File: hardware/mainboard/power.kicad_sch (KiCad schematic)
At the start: 18 parts, among them J105 Eurorack Power, U1 LM4040DBZ-10, U2 LD1117-3.3

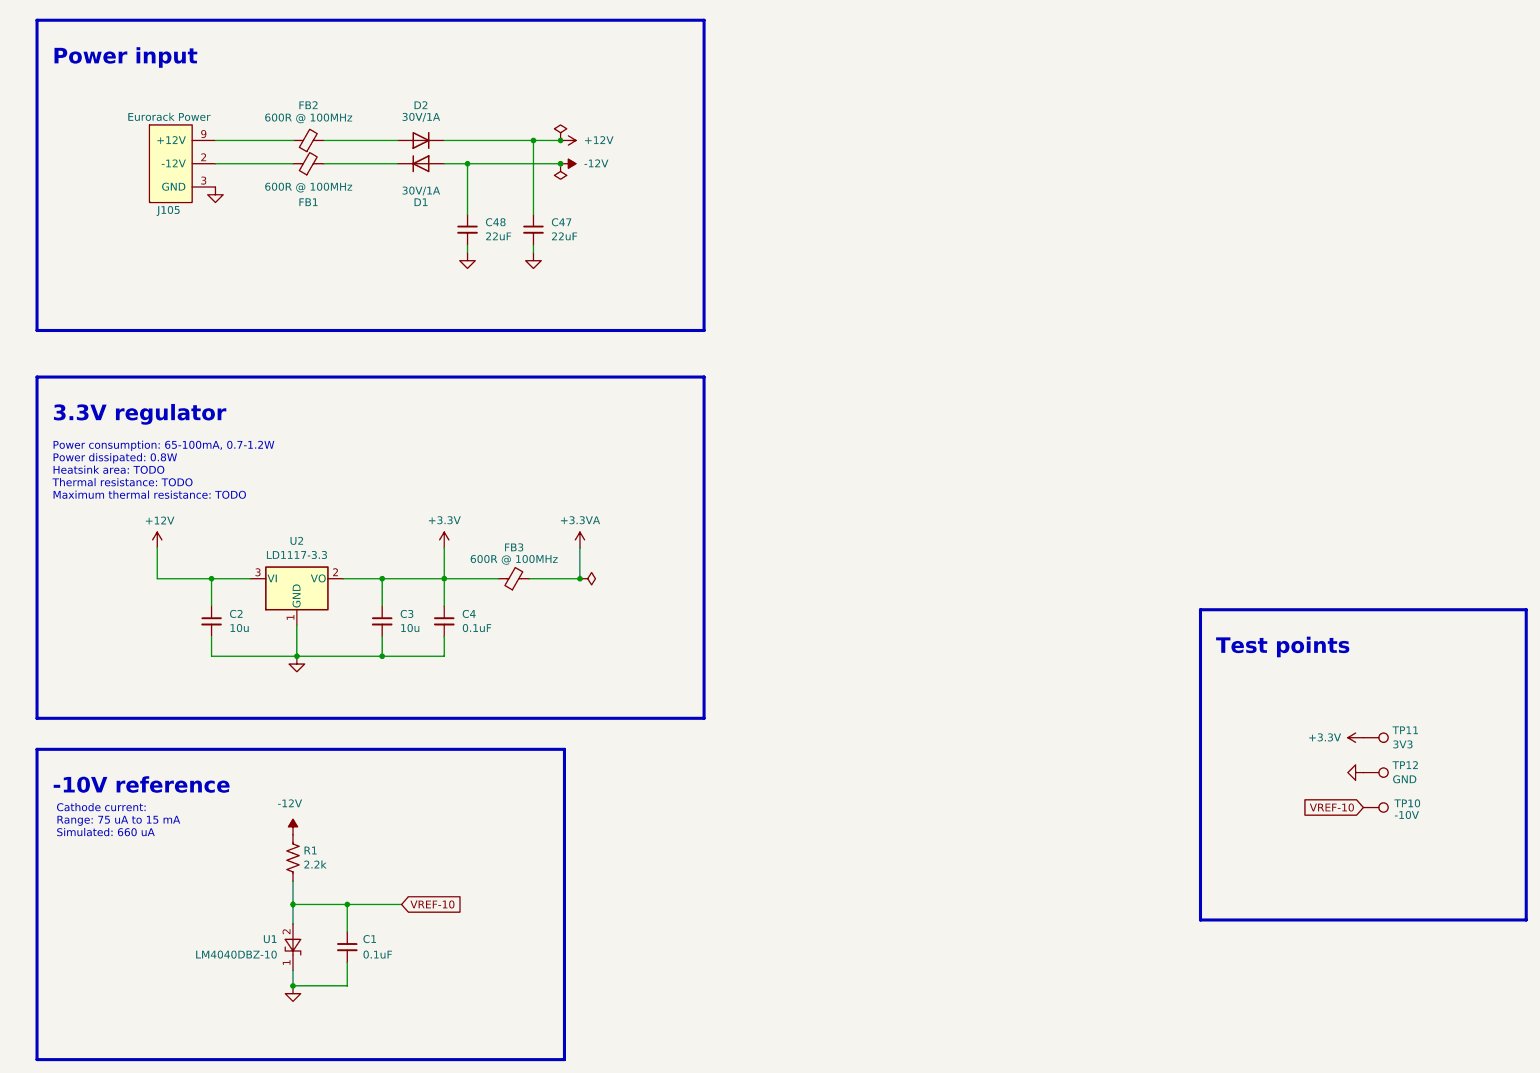
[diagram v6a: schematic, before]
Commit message: Reannotate schematic
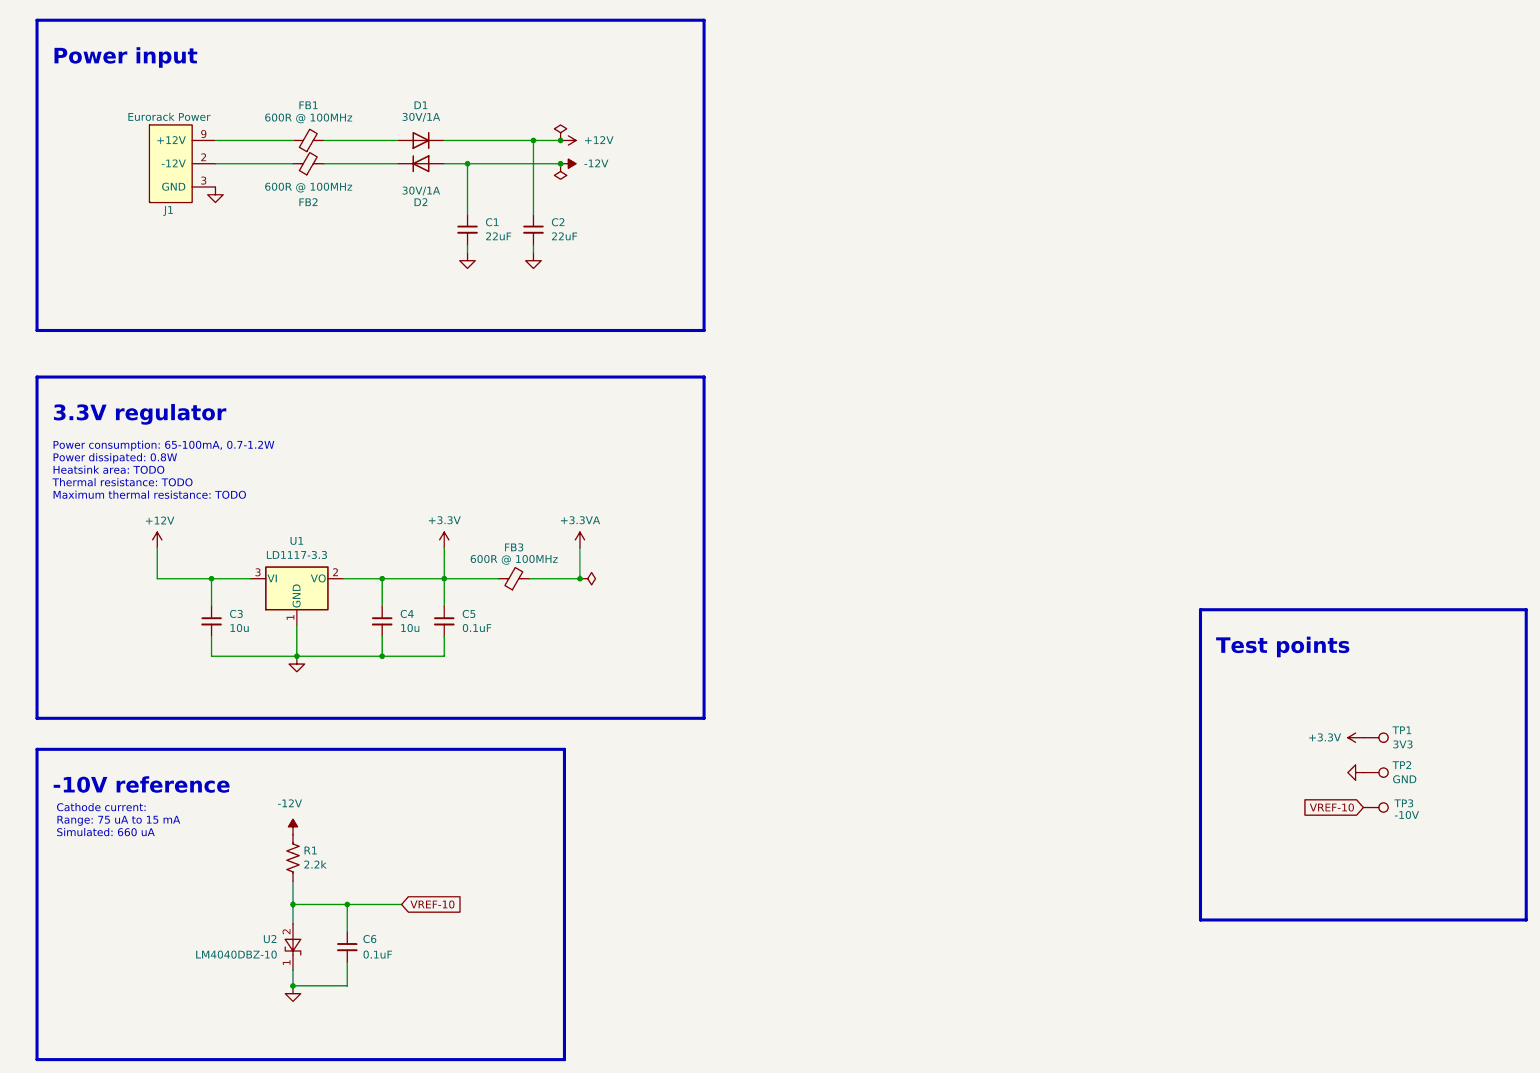
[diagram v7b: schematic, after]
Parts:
- renumbered C48 to C1, C47 to C2, C2 to C3, C3 to C4, C4 to C5, C1 to C6, D2 to D1, D1 to D2, FB2 to FB1, FB1 to FB2, J105 to J1, TP11 to TP1, TP12 to TP2, TP10 to TP3, U2 to U1, U1 to U2
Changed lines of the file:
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@@
   (symbol (lib_id "Device:D") (at 80.645 41.275 0) (unit 1)
     (in_bom yes) (on_board yes)
-    (property "Reference" "D1" (id 0) (at 80.645 47.625 0))
+    (property "Reference" "D2" (id 0) (at 80.645 47.625 0))
     (property "Value" "30V/1A" (id 1) (at 80.645 45.72 0))
     (property "Footprint" "winterbloom:D_SOD-123" (id 2) (at 80.645 41.275 0)
@@
   (symbol (lib_id "Device:D") (at 80.645 37.465 180) (unit 1)
     (in_bom yes) (on_board yes)
-    (property "Reference" "D2" (id 0) (at 80.645 31.75 0))
+    (property "Reference" "D1" (id 0) (at 80.645 31.75 0))
     (property "Value" "30V/1A" (id 1) (at 80.645 33.655 0))
     (property "Footprint" "winterbloom:D_SOD-123" (id 2) (at 80.645 37.465 0)
@@
   (symbol (lib_id "power:+12V") (at 103.505 37.465 270) (unit 1)
     (in_bom yes) (on_board yes)
-    (property "Reference" "#PWR06" (id 0) (at 99.695 37.465 0)
+    (property "Reference" "#PWR04" (id 0) (at 99.695 37.465 0)
       (effects (font (size 1.27 1.27)) hide)
     )
@@
   (symbol (lib_id "Regulator_Linear:LM1117-3.3") (at 60.325 109.22 0) (unit 1)
     (in_bom yes) (on_board yes)
-    (property "Reference" "U2" (id 0) (at 60.325 103.0732 0))
+    (property "Reference" "U1" (id 0) (at 60.325 103.0732 0))
     (property "Value" "LD1117-3.3" (id 1) (at 60.325 105.3846 0))
     (property "Footprint" "Package_TO_SOT_SMD:TO-252-3_TabPin2" (id 2) (at 60.325 109.22 0)
@@
   (symbol (lib_id "Device:C_Small") (at 46.355 116.205 0) (unit 1)
     (in_bom yes) (on_board yes)
-    (property "Reference" "C2" (id 0) (at 49.276 115.0366 0)
+    (property "Reference" "C3" (id 0) (at 49.276 115.0366 0)
       (effects (font (size 1.27 1.27)) (justify left))
     )
@@
   (symbol (lib_id "Device:C_Small") (at 74.295 116.205 0) (unit 1)
     (in_bom yes) (on_board yes)
-    (property "Reference" "C3" (id 0) (at 77.216 115.0366 0)
+    (property "Reference" "C4" (id 0) (at 77.216 115.0366 0)
       (effects (font (size 1.27 1.27)) (justify left))
     )
@@
   (symbol (lib_id "Device:C_Small") (at 84.455 116.205 0) (unit 1)
     (in_bom yes) (on_board yes)
-    (property "Reference" "C4" (id 0) (at 87.376 115.0366 0)
+    (property "Reference" "C5" (id 0) (at 87.376 115.0366 0)
       (effects (font (size 1.27 1.27)) (justify left))
     )
@@
   (symbol (lib_id "power:+3.3V") (at 84.455 104.14 0) (unit 1)
     (in_bom yes) (on_board yes)
-    (property "Reference" "#PWR012" (id 0) (at 84.455 107.95 0)
+    (property "Reference" "#PWR08" (id 0) (at 84.455 107.95 0)
       (effects (font (size 1.27 1.27)) hide)
     )
@@
   (symbol (lib_id "power:+3.3VA") (at 106.68 104.14 0) (unit 1)
     (in_bom yes) (on_board yes)
-    (property "Reference" "#PWR014" (id 0) (at 106.68 107.95 0)
+    (property "Reference" "#PWR09" (id 0) (at 106.68 107.95 0)
       (effects (font (size 1.27 1.27)) hide)
     )
@@
   (symbol (lib_id "power:GND") (at 60.325 121.92 0) (unit 1)
     (in_bom yes) (on_board yes)
-    (property "Reference" "#PWR09" (id 0) (at 60.325 128.27 0)
+    (property "Reference" "#PWR07" (id 0) (at 60.325 128.27 0)
       (effects (font (size 1.27 1.27)) hide)
     )
@@
   (symbol (lib_id "power:+12V") (at 37.465 104.14 0) (unit 1)
     (in_bom yes) (on_board yes)
-    (property "Reference" "#PWR08" (id 0) (at 37.465 107.95 0)
+    (property "Reference" "#PWR06" (id 0) (at 37.465 107.95 0)
       (effects (font (size 1.27 1.27)) hide)
     )
@@
   (symbol (lib_id "Device:FerriteBead_Small") (at 62.23 41.275 90) (unit 1)
     (in_bom yes) (on_board yes)
-    (property "Reference" "FB1" (id 0) (at 62.23 47.625 90))
+    (property "Reference" "FB2" (id 0) (at 62.23 47.625 90))
     (property "Value" "600R @ 100MHz" (id 1) (at 62.23 45.085 90))
     (property "Footprint" "Inductor_SMD:L_0603_1608Metric_Pad1.05x0.95mm_HandSolder" (id 2) (at 62.23 43.053 90)
@@
   (symbol (lib_id "Device:FerriteBead_Small") (at 62.23 37.465 90) (unit 1)
     (in_bom yes) (on_board yes)
-    (property "Reference" "FB2" (id 0) (at 62.23 31.75 90))
+    (property "Reference" "FB1" (id 0) (at 62.23 31.75 90))
     (property "Value" "600R @ 100MHz" (id 1) (at 62.23 33.7566 90))
     (property "Footprint" "Inductor_SMD:L_0603_1608Metric_Pad1.05x0.95mm_HandSolder" (id 2) (at 62.23 39.243 90)
@@
   (symbol (lib_id "winterbloom:LM4040DBZ-10") (at 59.69 169.545 270) (unit 1)
     (in_bom yes) (on_board yes)
-    (property "Reference" "U1" (id 0) (at 57.15 168.275 90)
+    (property "Reference" "U2" (id 0) (at 57.15 168.275 90)
       (effects (font (size 1.27 1.27)) (justify right))
     )
@@
   (symbol (lib_id "power:-12V") (at 59.69 151.13 0) (unit 1)
     (in_bom yes) (on_board yes)
-    (property "Reference" "#PWR03" (id 0) (at 59.69 148.59 0)
+    (property "Reference" "#PWR010" (id 0) (at 59.69 148.59 0)
       (effects (font (size 1.27 1.27)) hide)
     )
@@
   (symbol (lib_id "power:GND") (at 59.69 175.895 0) (unit 1)
     (in_bom yes) (on_board yes)
-    (property "Reference" "#PWR04" (id 0) (at 59.69 182.245 0)
+    (property "Reference" "#PWR011" (id 0) (at 59.69 182.245 0)
       (effects (font (size 1.27 1.27)) hide)
     )
@@
   (symbol (lib_id "Device:C_Small") (at 68.58 169.545 0) (unit 1)
     (in_bom yes) (on_board yes)
-    (property "Reference" "C1" (id 0) (at 71.12 168.275 0)
+    (property "Reference" "C6" (id 0) (at 71.12 168.275 0)
       (effects (font (size 1.27 1.27)) (justify left))
     )
@@
   (symbol (lib_id "Device:C_Small") (at 88.265 52.07 0) (unit 1)
     (in_bom yes) (on_board yes)
-    (property "Reference" "C48" (id 0) (at 91.186 50.9016 0)
+    (property "Reference" "C1" (id 0) (at 91.186 50.9016 0)
       (effects (font (size 1.27 1.27)) (justify left))
     )
@@
   (symbol (lib_id "power:GND") (at 46.99 45.085 0) (unit 1)
     (in_bom yes) (on_board yes)
-    (property "Reference" "#PWR0143" (id 0) (at 46.99 51.435 0)
+    (property "Reference" "#PWR01" (id 0) (at 46.99 51.435 0)
       (effects (font (size 1.27 1.27)) hide)
     )
@@
   (symbol (lib_id "power:PWR_FLAG") (at 106.68 109.22 270) (unit 1)
     (in_bom yes) (on_board yes)
-    (property "Reference" "#FLG0104" (id 0) (at 108.585 109.22 0)
+    (property "Reference" "#FLG03" (id 0) (at 108.585 109.22 0)
       (effects (font (size 1.27 1.27)) hide)
     )
@@
   (symbol (lib_id "power:GND") (at 234.95 140.97 270) (unit 1)
     (in_bom yes) (on_board yes)
-    (property "Reference" "#PWR039" (id 0) (at 228.6 140.97 0)
+    (property "Reference" "#PWR013" (id 0) (at 228.6 140.97 0)
       (effects (font (size 1.27 1.27)) hide)
     )
@@
   (symbol (lib_id "power:+3.3V") (at 234.95 135.255 90) (unit 1)
     (in_bom yes) (on_board yes)
-    (property "Reference" "#PWR038" (id 0) (at 238.76 135.255 0)
+    (property "Reference" "#PWR012" (id 0) (at 238.76 135.255 0)
       (effects (font (size 1.27 1.27)) hide)
     )
@@
   (symbol (lib_id "Connector:TestPoint") (at 234.95 146.685 270) (unit 1)
     (in_bom yes) (on_board yes)
-    (property "Reference" "TP10" (id 0) (at 240.03 146.05 90)
+    (property "Reference" "TP3" (id 0) (at 240.03 146.05 90)
       (effects (font (size 1.27 1.27)) (justify left))
     )
@@
   (symbol (lib_id "Connector:TestPoint") (at 234.95 135.255 270) (unit 1)
     (in_bom yes) (on_board yes)
-    (property "Reference" "TP11" (id 0) (at 239.7252 134.0866 90)
+    (property "Reference" "TP1" (id 0) (at 239.7252 134.0866 90)
       (effects (font (size 1.27 1.27)) (justify left))
     )
@@
   (symbol (lib_id "winterbloom:Eurorack_Power") (at 39.37 41.275 0) (unit 1)
     (in_bom yes) (on_board yes)
-    (property "Reference" "J105" (id 0) (at 39.37 48.895 0))
+    (property "Reference" "J1" (id 0) (at 39.37 48.895 0))
     (property "Value" "Eurorack Power" (id 1) (at 39.37 33.655 0))
     (property "Footprint" "winterbloom:Eurorack_Power_2x5_Shrouded" (id 2) (at 39.37 29.845 0)
@@
   (symbol (lib_id "power:GND") (at 99.06 55.88 0) (unit 1)
     (in_bom yes) (on_board yes)
-    (property "Reference" "#PWR01" (id 0) (at 99.06 62.23 0)
+    (property "Reference" "#PWR03" (id 0) (at 99.06 62.23 0)
       (effects (font (size 1.27 1.27)) hide)
     )
@@
   (symbol (lib_id "Device:C_Small") (at 99.06 52.07 0) (unit 1)
     (in_bom yes) (on_board yes)
-    (property "Reference" "C47" (id 0) (at 101.981 50.9016 0)
+    (property "Reference" "C2" (id 0) (at 101.981 50.9016 0)
       (effects (font (size 1.27 1.27)) (justify left))
     )
@@
   (symbol (lib_id "Connector:TestPoint") (at 234.95 140.97 270) (unit 1)
     (in_bom yes) (on_board yes)
-    (property "Reference" "TP12" (id 0) (at 239.7252 139.8016 90)
-      (effects (font (size 1.27 1.27)) (justify left))
-    )
+    (property "Reference" "TP2" (id 0) (at 239.7252 139.8016 90)
+      (effects (font (size 1.27 1.27)) (justify left))
+    )

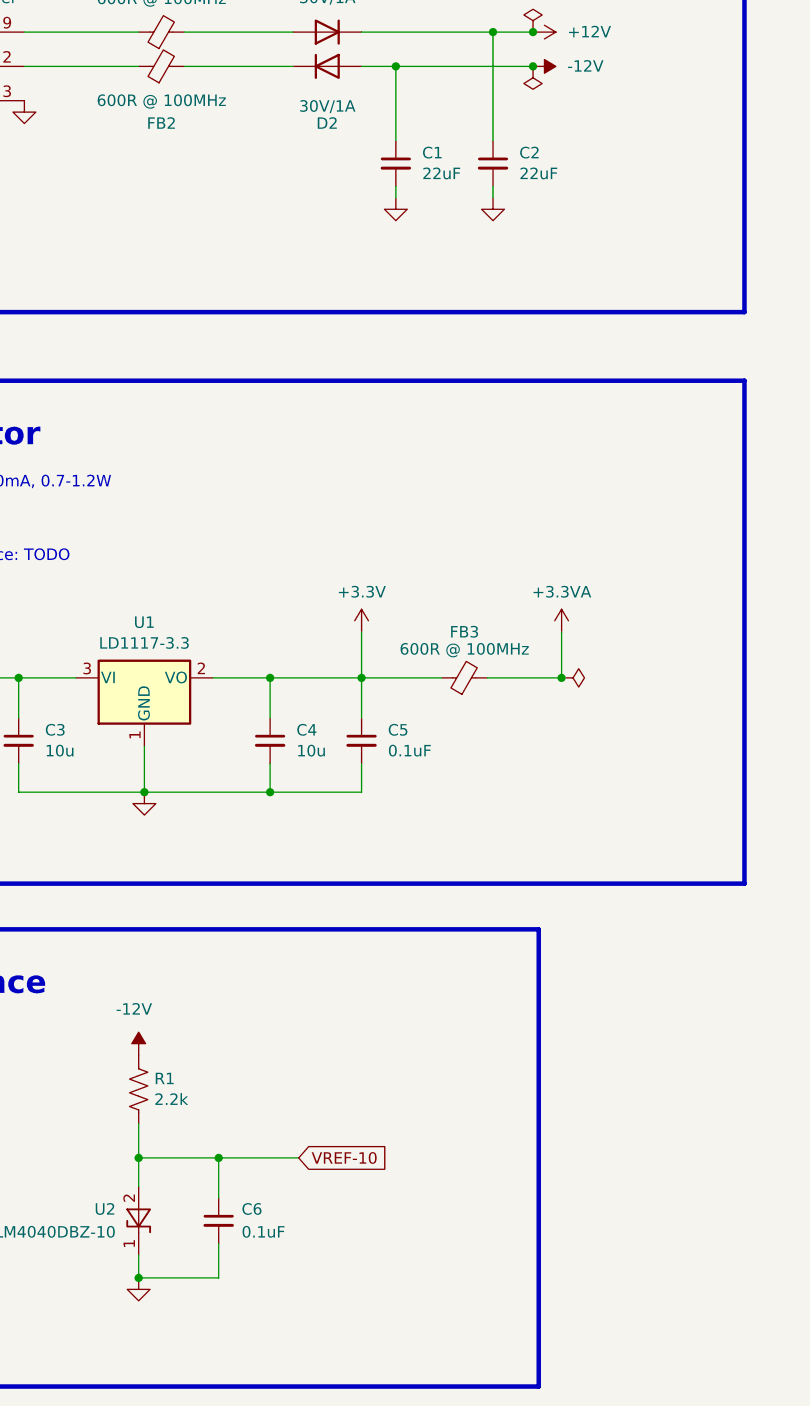
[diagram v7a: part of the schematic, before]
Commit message: Normalize component values
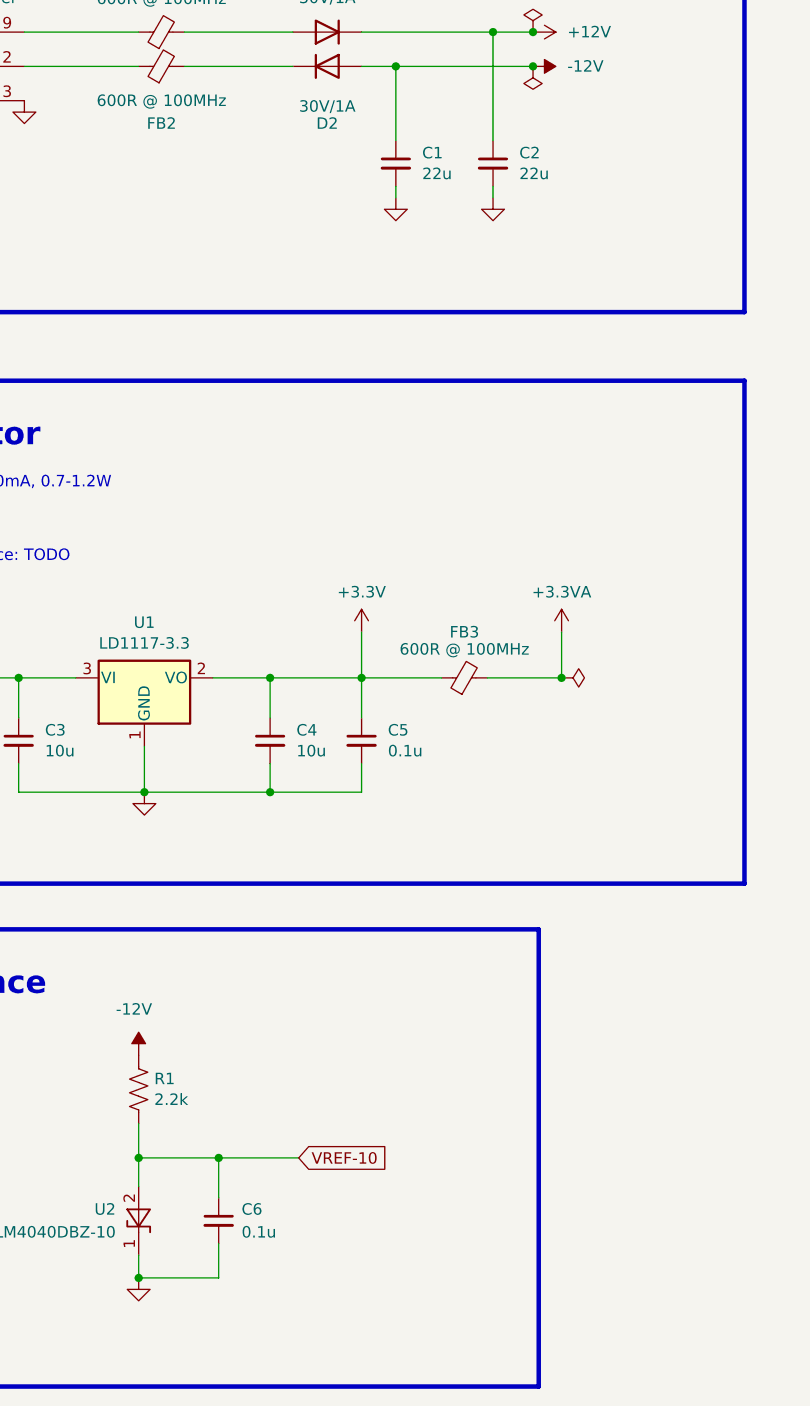
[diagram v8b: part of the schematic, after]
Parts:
- C1, C2: value 22uF -> 22u
- C5, C6: value 0.1uF -> 0.1u
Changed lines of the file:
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@@
       (effects (font (size 1.27 1.27)) (justify left))
     )
-    (property "Value" "0.1uF" (id 1) (at 87.376 117.348 0)
+    (property "Value" "0.1u" (id 1) (at 87.376 117.348 0)
       (effects (font (size 1.27 1.27)) (justify left))
     )
@@
       (effects (font (size 1.27 1.27)) (justify left))
     )
-    (property "Value" "0.1uF" (id 1) (at 71.12 170.815 0)
+    (property "Value" "0.1u" (id 1) (at 71.12 170.815 0)
       (effects (font (size 1.27 1.27)) (justify left))
     )
@@
       (effects (font (size 1.27 1.27)) (justify left))
     )
-    (property "Value" "22uF" (id 1) (at 91.186 53.213 0)
+    (property "Value" "22u" (id 1) (at 91.186 53.213 0)
       (effects (font (size 1.27 1.27)) (justify left))
     )
@@
       (effects (font (size 1.27 1.27)) (justify left))
     )
-    (property "Value" "22uF" (id 1) (at 101.981 53.213 0)
-      (effects (font (size 1.27 1.27)) (justify left))
-    )
+    (property "Value" "22u" (id 1) (at 101.981 53.213 0)
+      (effects (font (size 1.27 1.27)) (justify left))
+    )
